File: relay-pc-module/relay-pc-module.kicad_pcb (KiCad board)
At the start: 2 copper layers, 75 x 75.1 mm, 55 parts, among them J1 Conn_02x02_Odd_Even, J10 Conn_01x01, J2 DB9_Female, J3 Conn_01x01, J4 Screw_Terminal_01x03, J5 Screw_Terminal_01x03, J6 Screw_Terminal_01x03, J7 Conn_01x04, J8 Conn_01x04, J9 Conn_01x01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

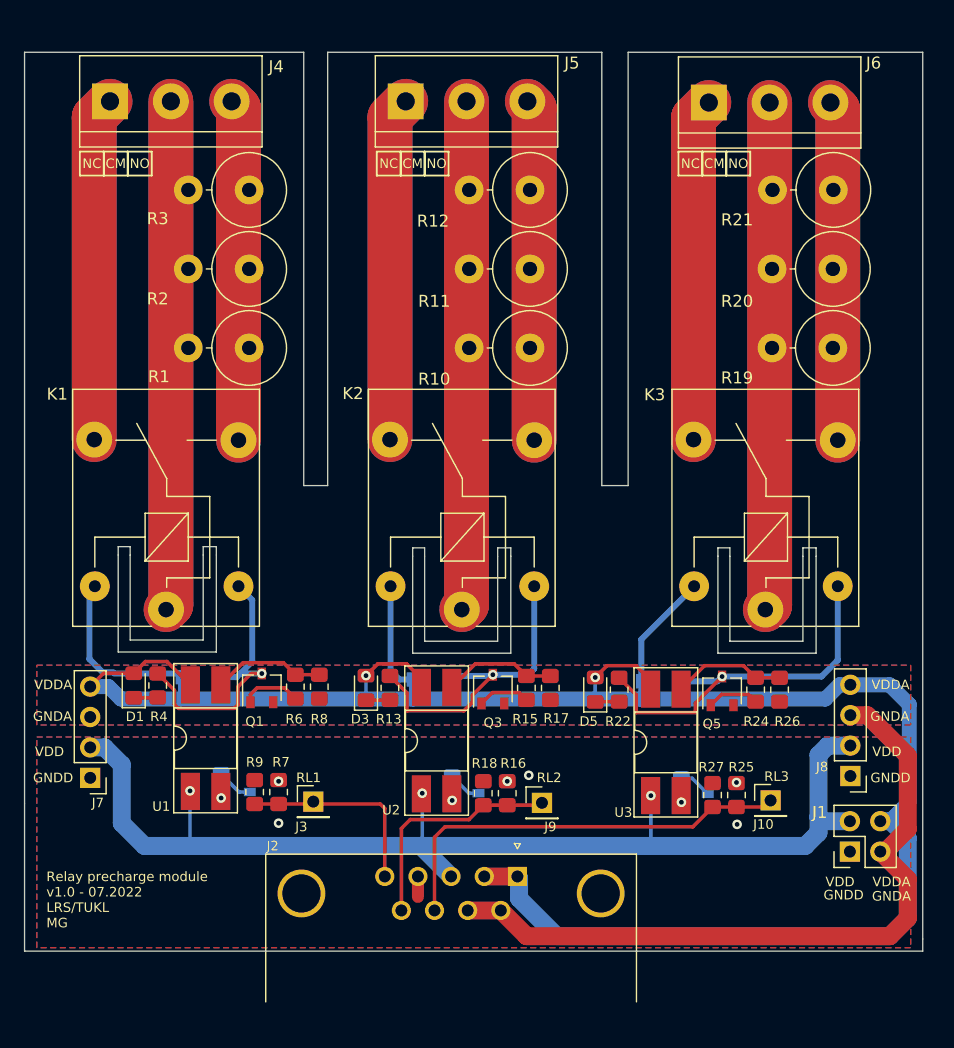
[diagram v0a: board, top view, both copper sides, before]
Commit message: Added 3D model and sim to relay precharge module
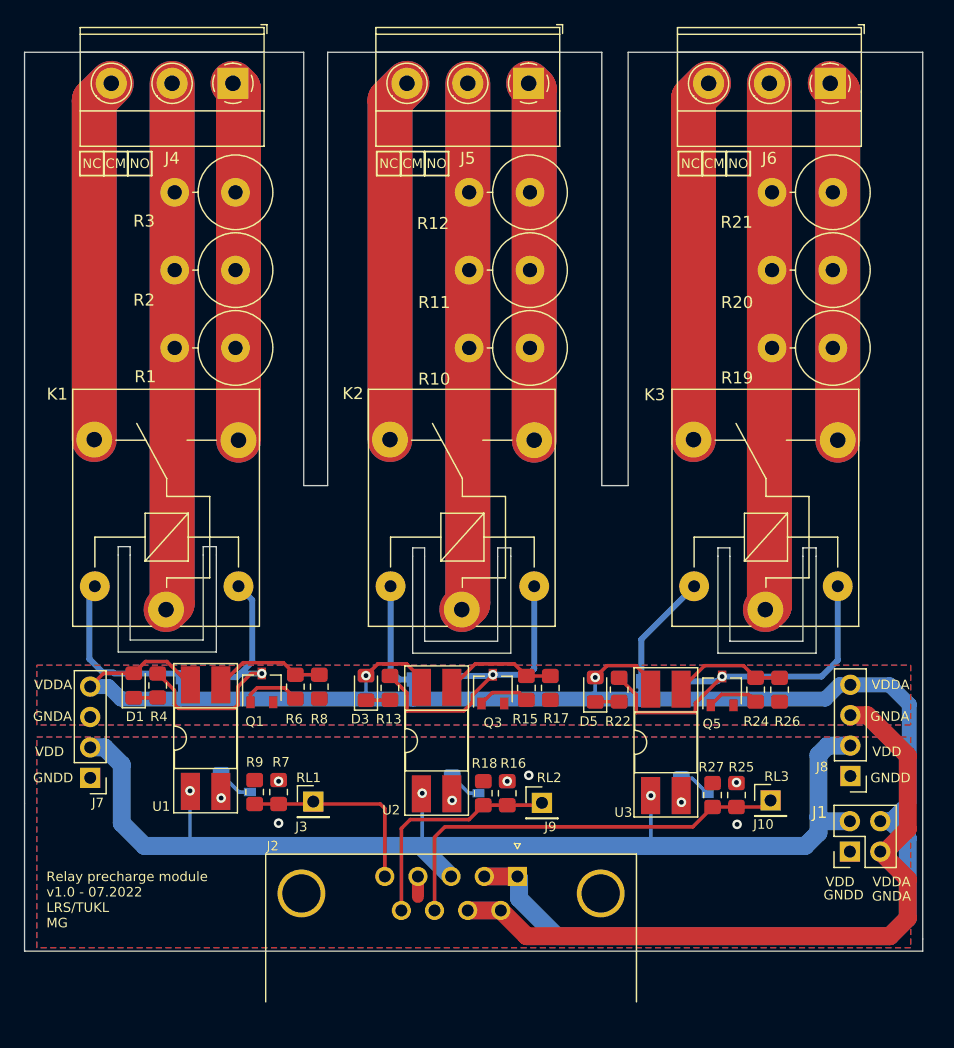
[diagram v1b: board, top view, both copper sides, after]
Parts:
- J4, J5, J6: footprint TerminalBlock:TerminalBlock_bornier-3_P5.08mm -> TerminalBlock_Phoenix:TerminalBlock_Phoenix_MKDS-1,5-3-5.08_1x03_P5.08mm_Horizontal
- moved J4 10.4 mm to (41.4, 25.3), turned to 180 degrees
- moved J5 10.4 mm to (66.1, 25.3), turned to 180 degrees
- moved J6 10.3 mm to (91.3, 25.3), turned to 180 degrees
- moved R3 1.16 mm to (41.6, 34.4)
- moved R2 1.14 mm to (41.6, 40.9)
- moved R1 1.14 mm to (41.6, 47.4)
- moved R21 0.20 mm to (91.5, 34.4)
- moved R12 0.20 mm to (66.2, 34.4)
- moved R11 0.10 mm to (66.2, 40.9)
- moved R20 0.10 mm to (91.5, 40.9)
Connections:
- J4 pad 1: /RL1_NC -> /RL1_NO
- J4 pad 3: /RL1_NO -> /RL1_NC
- J5 pad 1: /RL2_NC -> /RL2_NO
- J5 pad 3: /RL2_NO -> /RL2_NC
- J6 pad 1: /RL3_NC -> /RL3_NO
- J6 pad 3: /RL3_NO -> /RL3_NC
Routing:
- net /RL3_NO: track 56.9 -> 60.1 mm
- net /RL3_NC: track 57.4 -> 60.6 mm
- net /RL3_CM: track 85.0 -> 88.2 mm
- net /RL1_NC: track 57.6 -> 60.7 mm
- net /RL2_NC: track 57.6 -> 60.7 mm
- net /RL2_CM: track 85.2 -> 88.3 mm
- net /RL1_CM: track 85.2 -> 88.3 mm
- net /RL2_NO: track 57.1 -> 60.0 mm
- net /RL1_NO: track 57.1 -> 60.0 mm

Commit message: Finalizing relay-pc-module
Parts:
- added ?: , , F.Cu at (89.0, 92.2)
- added REF**: MountingHole_3.2mm_M3, MountingHole:MountingHole_3.2mm_M3, F.Cu at (34.0, 92.2)
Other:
- board text added: "Relay precharge module v1.0 - 07.2022"
- board text removed: "Relay precharge module v1.0 - 07.2022 LRS/TUKL MG"
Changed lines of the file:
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@@
     )
+  )
+  (footprint "" (layer "F.Cu")
+    (at 88.95 92.2)
+    (fp_text reference "" (at 0 0) (layer "F.SilkS")
+      (effects (font (size 1.27 1.27) (thickness 0.15)))
+    )
+    (fp_text value "" (at 0 0) (layer "F.SilkS")
+      (effects (font (size 1.27 1.27) (thickness 0.15)))
+    )
+    (pad "" np_thru_hole circle (at 0 0) (size 3.2 3.2) (drill 3.2) (layers *.Cu *.Mask))
   )
   (footprint "TerminalBlock_Phoenix:TerminalBlock_Phoenix_MKDS-1,5-3-5.08_1x03_P5.08mm_Horizontal" (layer "F.Cu")
@@
       (rotate (xyz 0 0 0))
     )
+  )
+  (footprint "MountingHole:MountingHole_3.2mm_M3" (layer "F.Cu")
+    (at 33.95 92.2)
+    (descr "Mounting Hole 3.2mm, no annular, M3")
+    (tags "mounting hole 3.2mm no annular m3")
+    (attr exclude_from_pos_files exclude_from_bom)
+    (fp_text reference "REF**" (at 3.95 0) (layer "F.SilkS") hide
+      (effects (font (size 1 1) (thickness 0.15)))
+    )
+    (fp_text value "MountingHole_3.2mm_M3" (at 0 4.2) (layer "F.Fab")
+      (effects (font (size 1 1) (thickness 0.15)))
+    )
+    (fp_text user "${REFERENCE}" (at 0 0) (layer "F.Fab")
+      (effects (font (size 1 1) (thickness 0.15)))
+    )
+    (fp_circle (center 0 0) (end 3.2 0) (layer "Cmts.User") (width 0.15) (fill none))
+    (fp_circle (center 0 0) (end 3.45 0) (layer "F.CrtYd") (width 0.05) (fill none))
+    (pad "" np_thru_hole circle (at 0 0) (size 3.2 3.2) (drill 3.2) (layers *.Cu *.Mask))
   )
   (footprint "Resistor_THT:R_Axial_DIN0617_L17.0mm_D6.0mm_P5.08mm_Vertical" (layer "F.Cu")
@@
     (effects (font (size 0.8 0.8) (thickness 0.15)))
   )
-  (gr_text "Relay precharge module\nv1.0 - 07.2022\nLRS/TUKL\nMG\n" (at 25.8 93.5) (layer "F.SilkS")
+  (gr_text "Relay precharge module\nv1.0 - 07.2022\n" (at 25.2 88.05) (layer "F.SilkS")
     (effects (font (size 0.8 0.8) (thickness 0.15)) (justify left))
   )

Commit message: Added LEDs to relay pc module
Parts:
- added D7: LED, LED_SMD:LED_0805_2012Metric_Pad1.15x1.40mm_HandSolder, F.Cu at (26.1, 71.8)
- added D8: LED, LED_SMD:LED_0805_2012Metric_Pad1.15x1.40mm_HandSolder, F.Cu at (26.4, 86.2)
- added R28: 2k, Resistor_SMD:R_0805_2012Metric_Pad1.20x1.40mm_HandSolder, B.Cu at (26.1, 71.8)
- added R29: 2k, Resistor_SMD:R_0805_2012Metric_Pad1.20x1.40mm_HandSolder, B.Cu at (26.4, 86.2)
- moved ? 3.50 mm to (85.5, 92.2)
- moved REF** 3.50 mm to (37.5, 92.2)
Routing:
- net VDD: track 96.9 -> 104.0 mm
- net VDDA: track 194.8 -> 200.7 mm
- net GNDA: track 60.2 -> 63.3 mm
- net Net-(D8-Pad1): vias 0 -> 1
- net Net-(D7-Pad1): vias 0 -> 1

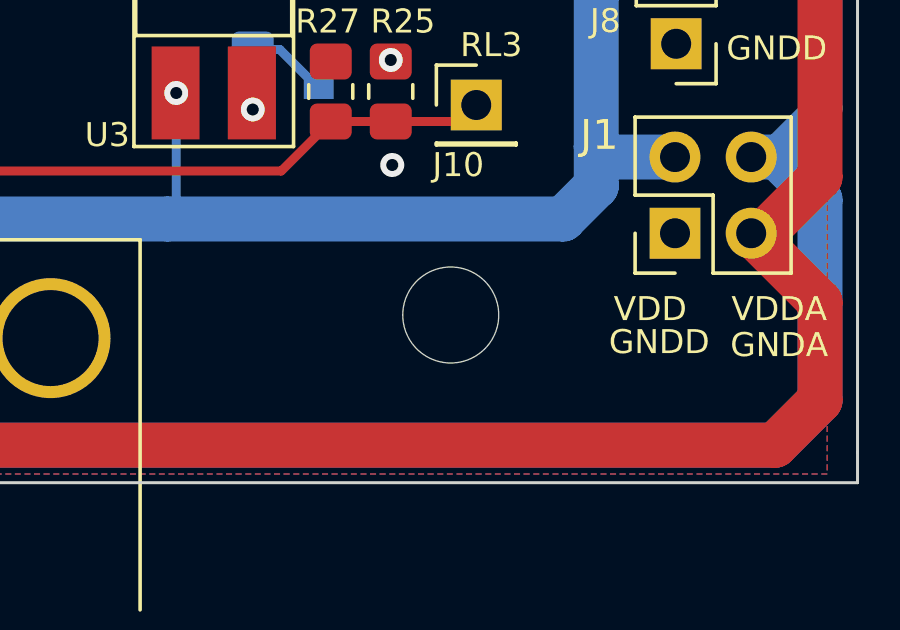
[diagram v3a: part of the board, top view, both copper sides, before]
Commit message: Added/fixed mounting holes
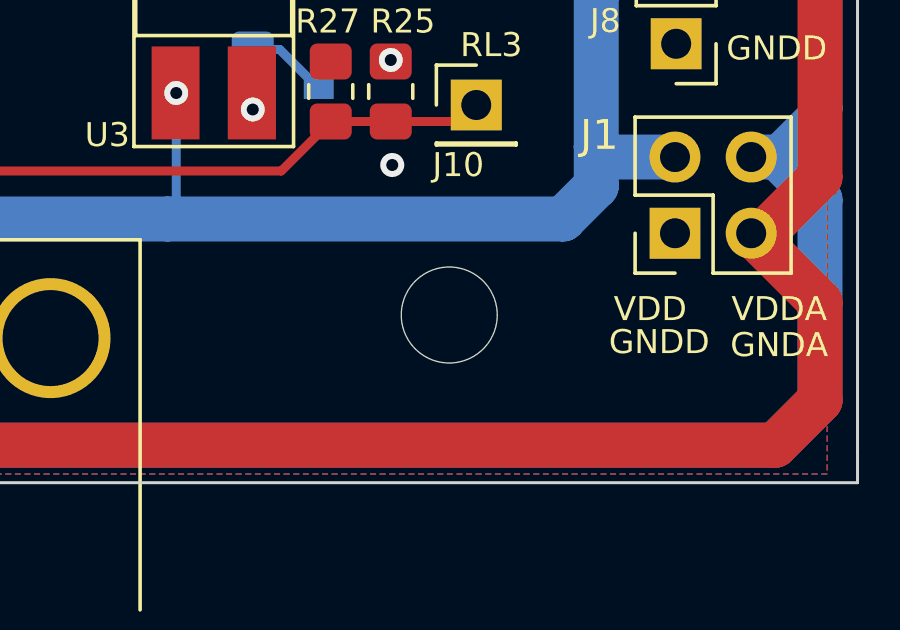
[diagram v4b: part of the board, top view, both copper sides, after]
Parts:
- removed ?: , 
- added REF**: MountingHole_3.2mm_M3, MountingHole:MountingHole_3.2mm_M3, F.Cu at (85.4, 92.2)
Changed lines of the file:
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@@
     )
-  )
-  (footprint "" (layer "F.Cu")
-    (at 85.45 92.2)
-    (fp_text reference "" (at 0 0) (layer "F.SilkS")
-      (effects (font (size 1.27 1.27) (thickness 0.15)))
-    )
-    (fp_text value "" (at 0 0) (layer "F.SilkS")
-      (effects (font (size 1.27 1.27) (thickness 0.15)))
-    )
-    (pad "" np_thru_hole circle (at 0 0) (size 3.2 3.2) (drill 3.2) (layers *.Cu *.Mask))
   )
   (footprint "TerminalBlock_Phoenix:TerminalBlock_Phoenix_MKDS-1,5-3-5.08_1x03_P5.08mm_Horizontal" (layer "F.Cu")
@@
     )
   )
+  (footprint "MountingHole:MountingHole_3.2mm_M3" (layer "F.Cu")
+    (at 85.4 92.2)
+    (descr "Mounting Hole 3.2mm, no annular, M3")
+    (tags "mounting hole 3.2mm no annular m3")
+    (attr exclude_from_pos_files exclude_from_bom)
+    (fp_text reference "REF**" (at 3.95 0) (layer "F.SilkS") hide
+      (effects (font (size 1 1) (thickness 0.15)))
+    )
+    (fp_text value "MountingHole_3.2mm_M3" (at 0 4.2) (layer "F.Fab")
+      (effects (font (size 1 1) (thickness 0.15)))
+    )
+    (fp_text user "${REFERENCE}" (at 0 0) (layer "F.Fab")
+      (effects (font (size 1 1) (thickness 0.15)))
+    )
+    (fp_circle (center 0 0) (end 3.2 0) (layer "Cmts.User") (width 0.15) (fill none))
+    (fp_circle (center 0 0) (end 3.45 0) (layer "F.CrtYd") (width 0.05) (fill none))
+    (pad "" np_thru_hole circle (at 0 0) (size 3.2 3.2) (drill 3.2) (layers *.Cu *.Mask))
+  )
   (footprint "Package_TO_SOT_SMD:SOT-23W" (layer "F.Cu")

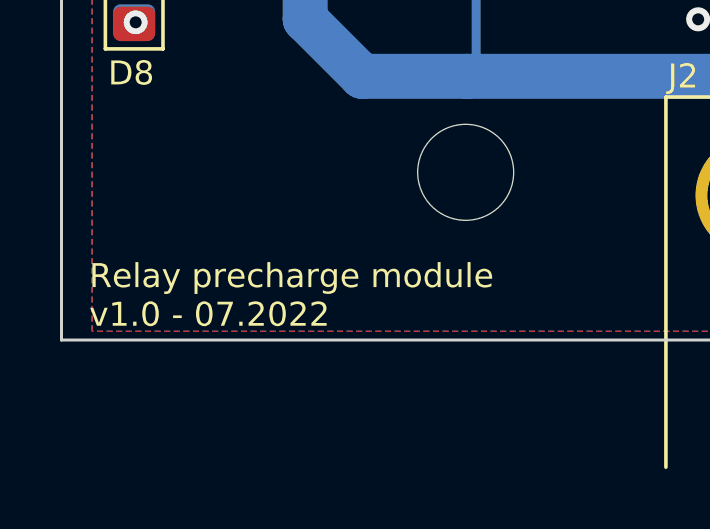
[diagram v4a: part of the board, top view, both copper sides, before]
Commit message: Updated boards with dates, silk, mounting holes
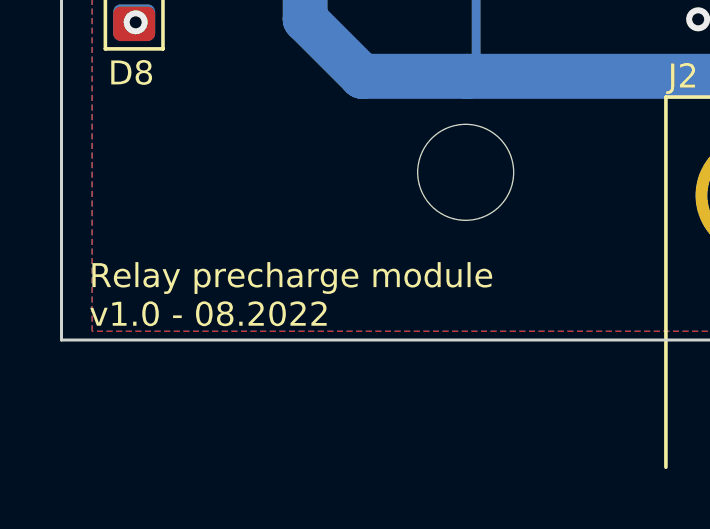
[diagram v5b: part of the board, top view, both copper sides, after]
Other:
- board text added: "Relay precharge module v1.0 - 08.2022"
- board text removed: "Relay precharge module v1.0 - 07.2022"
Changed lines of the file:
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@@
     (effects (font (size 0.8 0.8) (thickness 0.15)))
   )
-  (gr_text "Relay precharge module\nv1.0 - 07.2022\n" (at 24.9 96.3) (layer "F.SilkS")
+  (gr_text "Relay precharge module\nv1.0 - 08.2022\n" (at 24.9 96.3) (layer "F.SilkS")
     (effects (font (size 0.8 0.8) (thickness 0.15)) (justify left))
   )

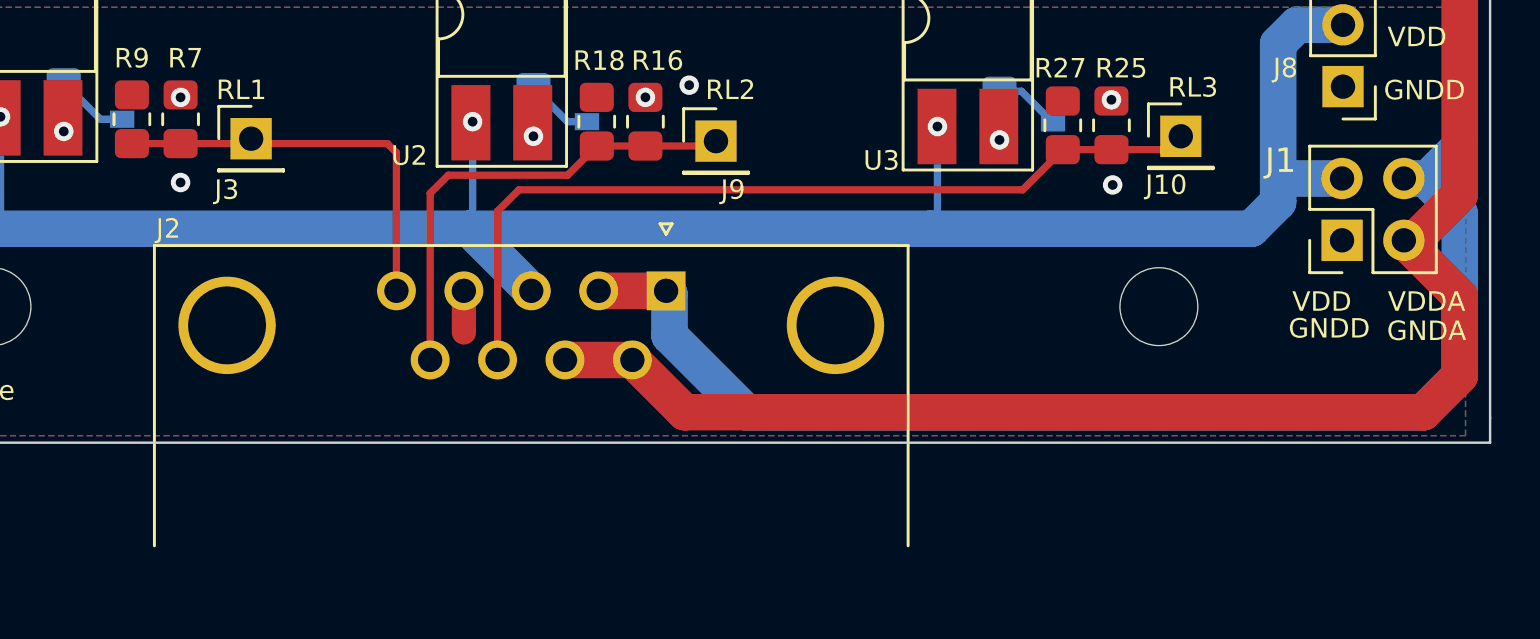
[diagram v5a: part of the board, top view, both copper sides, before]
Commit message: Removed db9 connector from relay-pc module
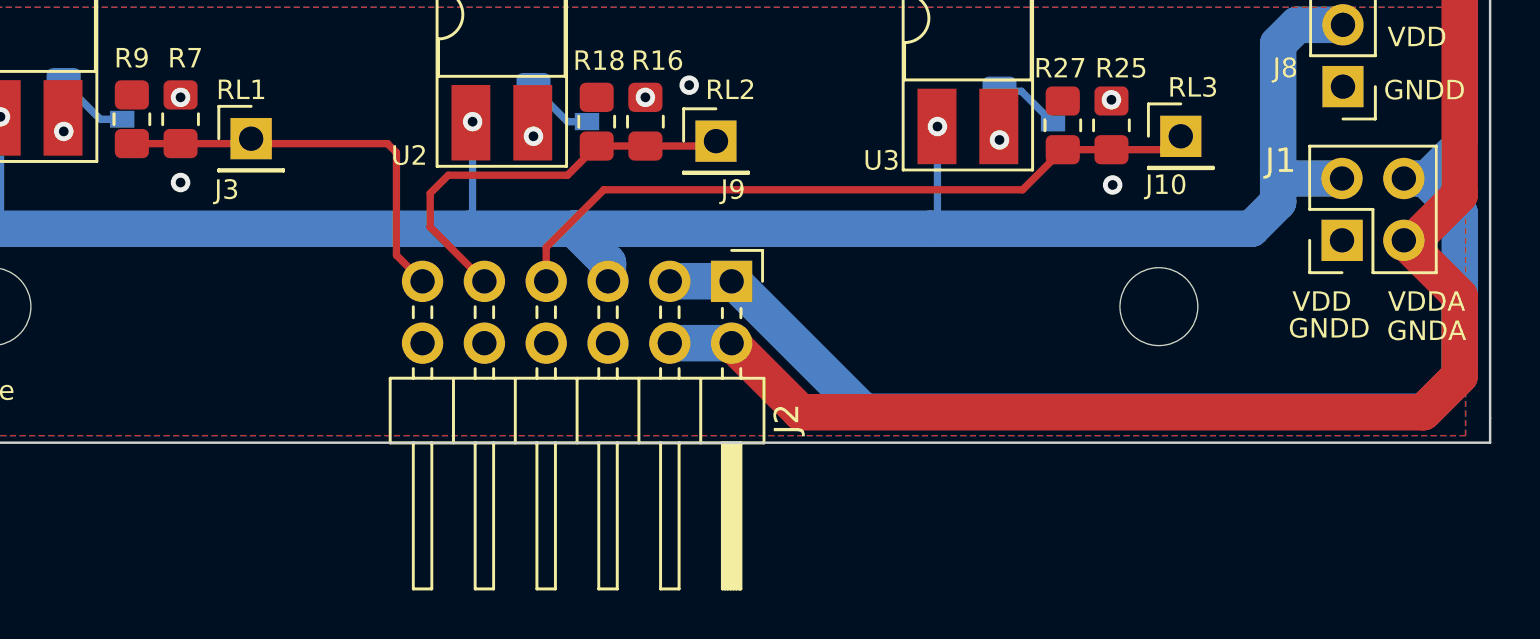
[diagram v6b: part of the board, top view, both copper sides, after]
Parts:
- J2: value DB9_Female -> Conn_02x06_Odd_Even; footprint Connector_Dsub:DSUB-9_Female_Horizontal_P2.77x2.84mm_EdgePinOffset7.70mm_Housed_MountingHolesOffset9.12mm -> Connector_PinHeader_2.54mm:PinHeader_2x06_P2.54mm_Horizontal
- moved J2 2.72 mm to (67.8, 91.2), turned to -90 degrees
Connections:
- J2 pad 2: VDDA -> GNDA
- J2 pad 3: VDD -> VDDA
- J2 pad 4: GNDD -> GNDA
- J2 pad 5: /RL1 -> VDD
- J2 pad 6: GNDA -> GNDD
- J2 pad 7: GNDA -> /RL3
- J2 pad 8: /RL3 -> GNDD
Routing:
- net /RL3: track 35.5 -> 29.4 mm
- net GNDA: track 63.3 -> 59.3 mm
- net VDDA: track 200.7 -> 196.9 mm
- net /RL2: track 19.8 -> 17.5 mm
- net GNDD: track 1.71 -> 0.00 mm
- net VDD: track 104.0 -> 103.2 mm
